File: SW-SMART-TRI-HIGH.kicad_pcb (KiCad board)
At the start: 2 copper layers, 72 x 69 mm, 53 parts, among them J1 SWLINK, J2 USART1, J3 POWER_OUT, SW0 BTS7002-1EPP, SW1 BTS7002-1EPP, SW2 BTS7002-1EPP, U1 STM32G0B1KBTx, U4 MCP2562-E-SN

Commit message: fattened up some tracks
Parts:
- J3: value POWER_OUT -> POWER OUT
- J4: renamed from POWER_IN1; value PWRIN -> POWER IN
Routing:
- net /SW2OUT: vias 0 -> 20
- net /SW1OUT: vias 0 -> 20
- net /SW0OUT: vias 0 -> 21

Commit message: switch to smps for 5v, adjust CAN and SWD pin connections
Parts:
- removed C5V0: 10u, Capacitor_SMD:C_0805_2012Metric_Pad1.18x1.45mm_HandSolder
- removed CVIN1: 10u, Capacitor_SMD:C_1206_3216Metric_Pad1.33x1.80mm_HandSolder
- removed VR5V0: NCV1117ST50, PCM_SparkFun-Semiconductor-Standard:SOT-223-3_TabPin2
- added C15: 100n, Capacitor_SMD:C_0603_1608Metric_Pad1.08x0.95mm_HandSolder, F.Cu at (120.5, 117.9)
- added CIN1: 10u, Capacitor_SMD:C_1210_3225Metric_Pad1.33x2.70mm_HandSolder, F.Cu at (125.7, 128.3)
- added CIN2: 100n, Capacitor_SMD:C_0603_1608Metric_Pad1.08x0.95mm_HandSolder, F.Cu at (120.5, 120.4)
- added COUT3: 10u, Capacitor_SMD:C_0805_2012Metric_Pad1.18x1.45mm_HandSolder, F.Cu at (133.4, 118.1)
- added COUT4: 10u, Capacitor_SMD:C_0805_2012Metric_Pad1.18x1.45mm_HandSolder, F.Cu at (133.4, 121.1)
- added L1: 8.2 uH 55.2 mOhm, SamacSys_Parts:SRP5030HMT2R2M, F.Cu at (126.8, 121.4)
- added RFBB1: 22K1, Resistor_SMD:R_0603_1608Metric_Pad0.98x0.95mm_HandSolder, F.Cu at (120.5, 122.9)
- added RFBT1: 115K, Resistor_SMD:R_0603_1608Metric_Pad0.98x0.95mm_HandSolder, F.Cu at (120.5, 125.4)
- added U3: LMR54410, Package_TO_SOT_SMD:SOT-23-6, F.Cu at (131.3, 128.6)
- CAN1: value H GND L -> G H L; footprint TerminalBlock_Phoenix:TerminalBlock_Phoenix_MKDS-1,5-3-5.08_1x03_P5.08mm_Horizontal -> TerminalBlock_Phoenix:TerminalBlock_Phoenix_MPT-0,5-3-2.54_1x03_P2.54mm_Horizontal
- moved C3V0 8.63 mm to (142.2, 123.8)
- moved CDIV1 5.90 mm to (123.4, 110.4)
- moved RVDIV1 5.90 mm to (123.4, 113.4)
- moved RVDIV2 5.90 mm to (123.4, 111.9)
- moved VR3V3 5.37 mm to (137.6, 127.8), turned to 0 degrees
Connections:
- CAN1 pad 1: /CAN_H -> GND
- CAN1 pad 2: GND -> /CAN_H
- J1 pad 1: +3.3V -> /NRST
- J1 pad 2: /NRST -> +3.3V
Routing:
- net +5V: track 62.3 -> 27.1 mm
- net /VS: track 20.5 -> 4.70 mm
- net GND: track 99.5 -> 86.7 mm, vias 24 -> 22
- net +3.3V: track 70.0 -> 57.4 mm
- net +12V: track 3.03 -> 0.00 mm
- net /NRST: track 16.7 -> 15.9 mm, vias 2 -> 1

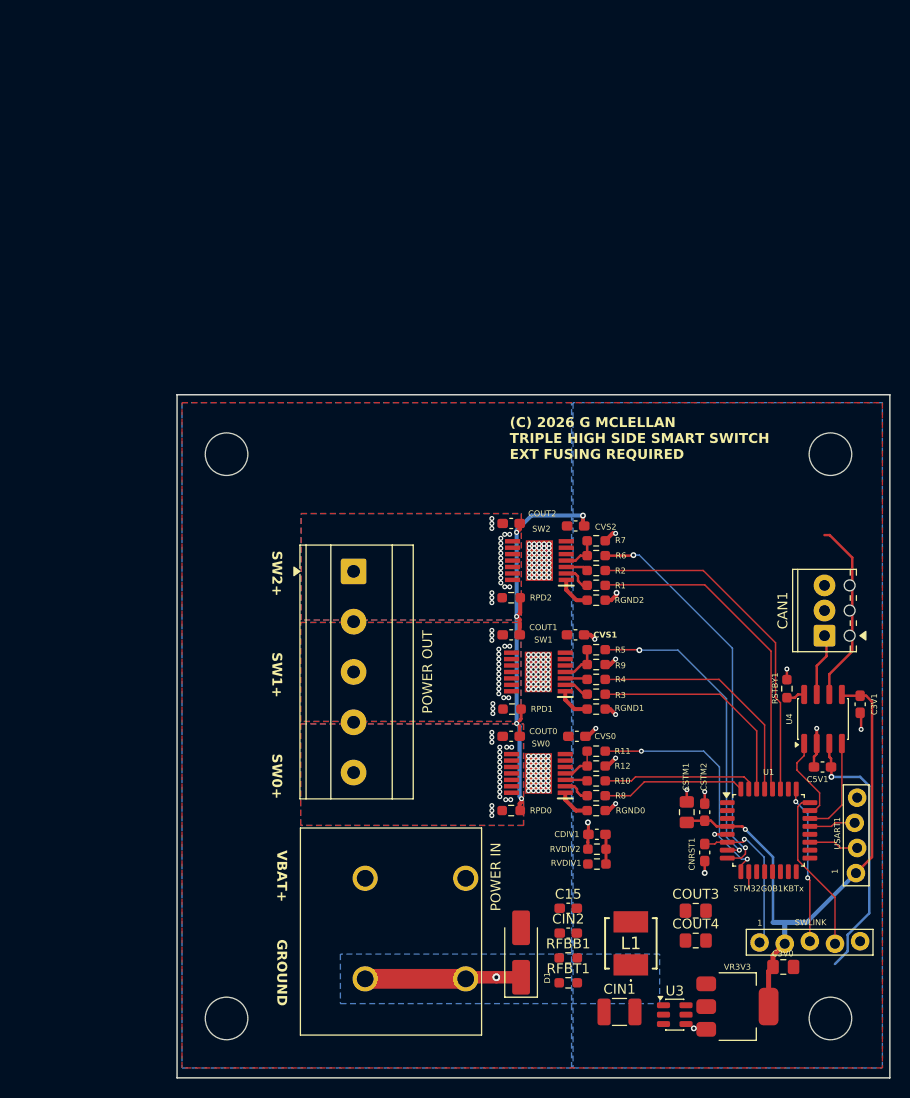
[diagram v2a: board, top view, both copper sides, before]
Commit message: improve ground connections, cleanup silkscreen
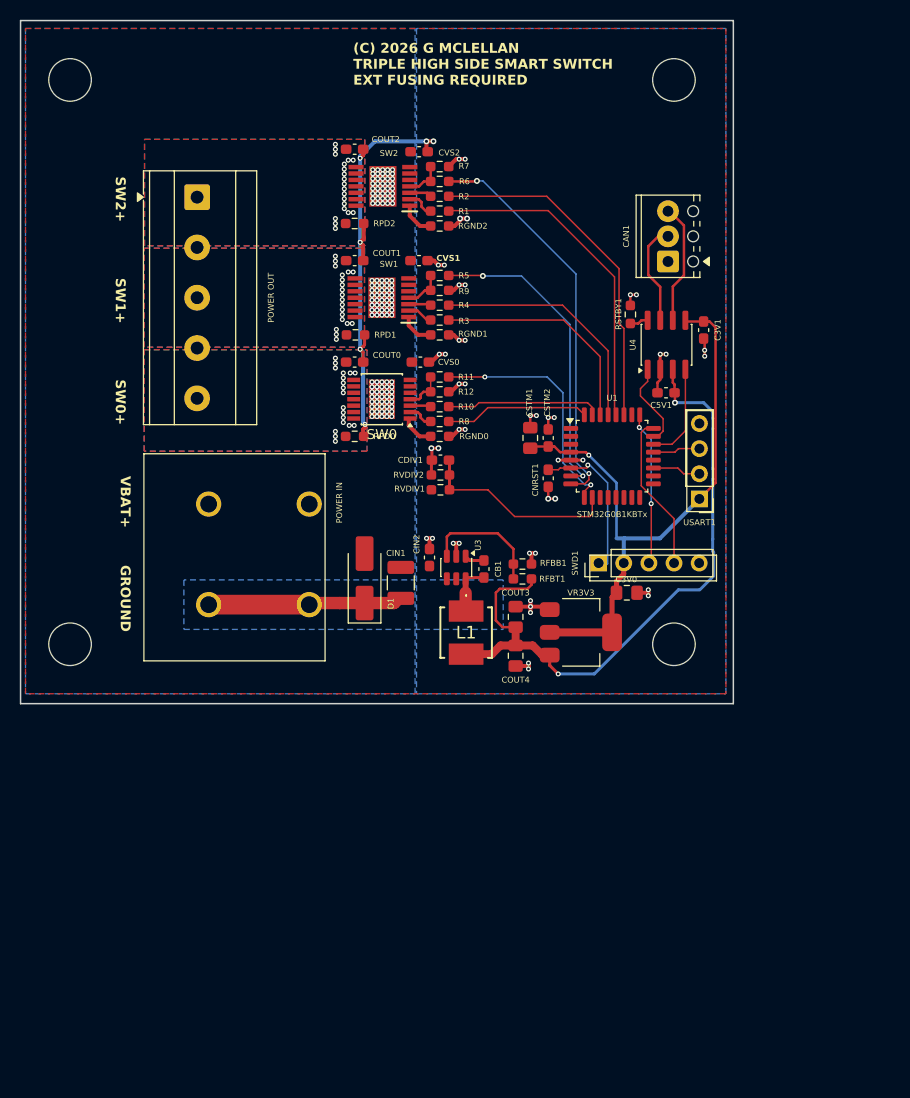
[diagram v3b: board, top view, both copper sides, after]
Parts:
- SW0: footprint SamacSys_Parts:SOP65P600X115-15N -> Package_SO:Infineon_PG-TSDSO-14-22
- SWD1: renamed from J1; value SWLINK -> RST 3V3 CLK DIO GND; footprint PCM_SparkFun-Connector:1x05_P2.54mm_Locking -> Connector_PinHeader_2.54mm:PinHeader_1x05_P2.54mm_Vertical
- USART1: renamed from J2; value USART1 -> 3V3 TX RX GND; footprint PCM_SparkFun-Connector:1x04_P2.54mm_Locking -> Connector_PinHeader_2.54mm:PinHeader_1x04_P2.54mm_Vertical
- moved U3 50.3 mm to (109.2, 83.5), turned to -90 degrees
- moved CIN1 48.6 mm to (103.6, 85.0), turned to -90 degrees
- moved SWD1 41.6 mm to (123.6, 83.0), turned to 90 degrees
- moved RFBT1 41.1 mm to (115.9, 84.6), turned to 180 degrees
- moved CDIV1 41.0 mm to (107.6, 72.6)
- moved RVDIV1 41.0 mm to (107.6, 75.6)
- moved RVDIV2 41.0 mm to (107.6, 74.1)
- moved C3V1 41.0 mm to (134.2, 59.5)
- moved J3 41.0 mm to (83.0, 46.0)
- moved C3V0 41.0 mm to (126.4, 86.0)
- moved CAN1 41.0 mm to (130.6, 52.5)
- moved CNRST1 41.0 mm to (118.5, 74.4)
- moved COUT0 41.0 mm to (98.9, 62.7)
- moved COUT1 41.0 mm to (98.9, 52.5)
- moved COUT2 41.0 mm to (98.9, 41.2)
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- renumbered C15 to CB1
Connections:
- net Net-(U3-FB) renamed /FB
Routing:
- net +5V: track 27.1 -> 67.0 mm
- net GND: track 86.7 -> 113.0 mm, vias 22 -> 51
- net /VS: track 4.70 -> 20.3 mm
- net /FB: track 0.00 -> 12.5 mm
- net /CAN_L: track 18.6 -> 12.2 mm
- net +3.3V: track 57.4 -> 63.2 mm
- net /SW: track 0.00 -> 4.94 mm
- net /CAN_H: track 6.43 -> 10.4 mm
- net /CB: track 0.00 -> 2.03 mm
- net /SW0IS_PD: track 4.02 -> 4.81 mm
- net /SWDIO: track 16.8 -> 16.2 mm
- net /SW0IS: track 24.6 -> 23.9 mm
- net /SW0OUT: vias 21 -> 19
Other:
- board text removed: "1"

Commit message: fixed some footprints, made the +12v pour a bit bigger on the bottom side
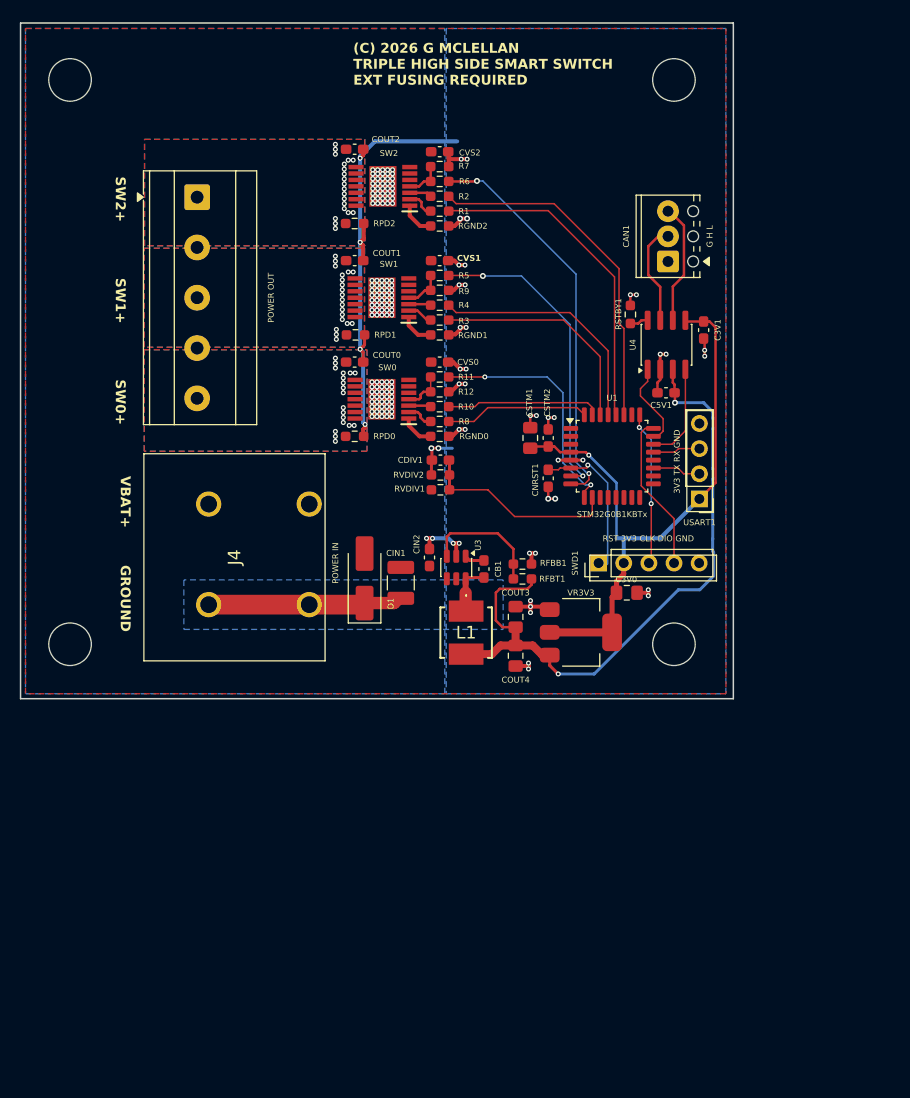
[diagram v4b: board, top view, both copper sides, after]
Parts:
- SW0: footprint Package_SO:Infineon_PG-TSDSO-14-22 -> SamacSys_Parts:SOP65P600X115-15N
- moved CVS1 2.08 mm to (107.5, 52.5)
- moved CVS2 2.08 mm to (107.5, 41.5)
- moved CVS0 1.95 mm to (107.5, 62.7)
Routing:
- net GND: track 113.0 -> 121.0 mm, vias 51 -> 49
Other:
- board size 72 x 69 mm -> 72 x 68.2 mm

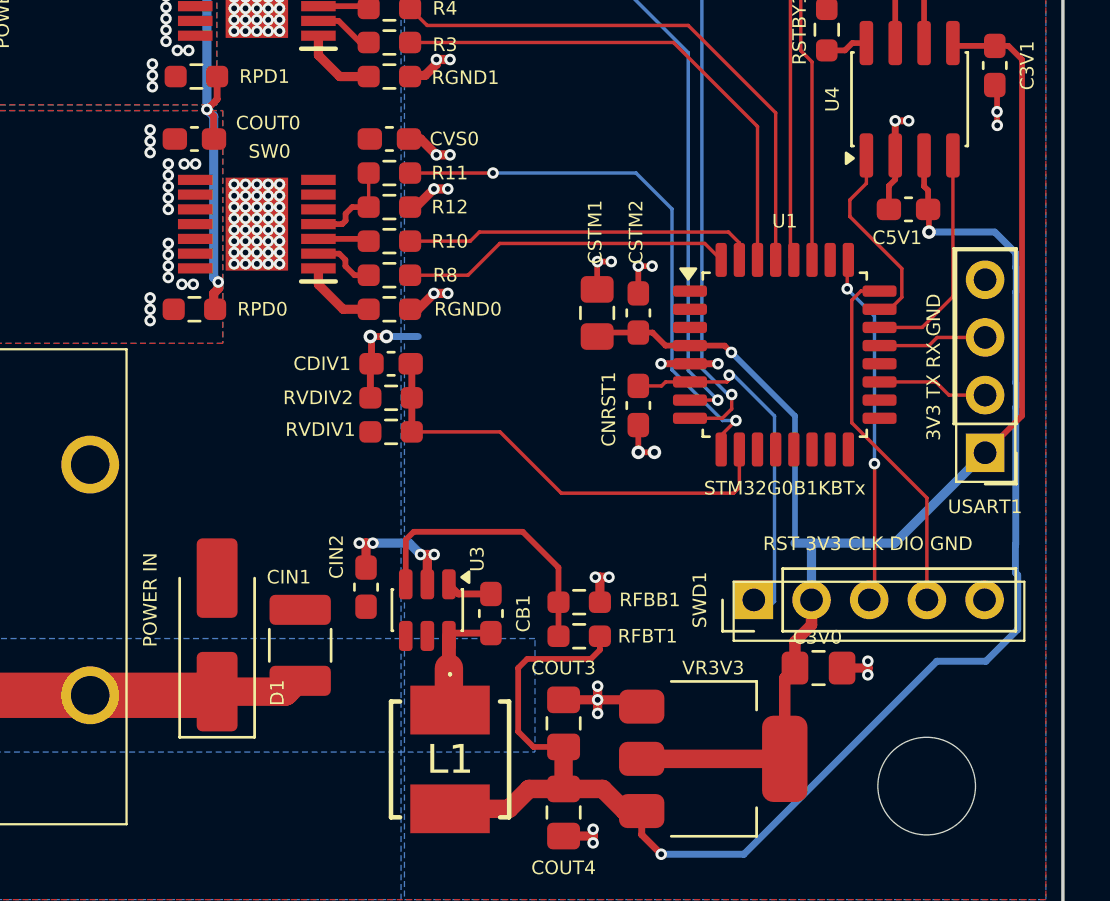
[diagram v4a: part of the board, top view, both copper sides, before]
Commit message: add 8mhz XO, fix some footprint issues
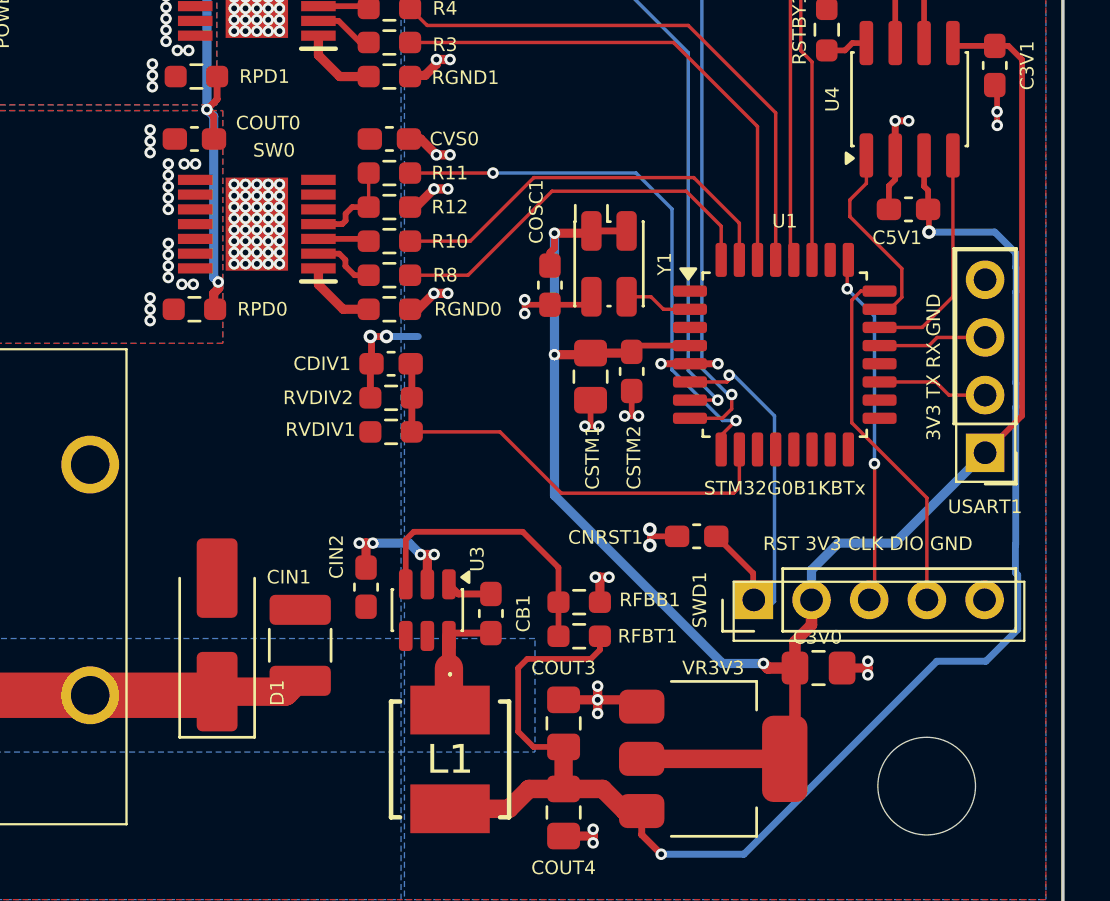
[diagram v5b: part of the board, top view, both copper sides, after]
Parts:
- added COSC1: 100n, Capacitor_SMD:C_0603_1608Metric_Pad1.08x0.95mm_HandSolder, F.Cu at (114.6, 69.1)
- added Y1: 8MHz, 3525_4pin_OSC:Oscillator_SMD_XO-4Pin_3.2x2.5mm_HandSoldering, F.Cu at (117.2, 68.2)
- moved CNRST1 6.31 mm to (121.1, 80.2), turned to 180 degrees
- moved CSTM1 2.82 mm to (116.4, 73.2), turned to -90 degrees
- moved CSTM2 2.59 mm to (118.2, 72.9), turned to -90 degrees
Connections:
- U1 pad 2: unconnected-(U1-PC14-Pad2) -> /OSC
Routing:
- net +3.3V: track 63.2 -> 82.2 mm, vias 1 -> 3
- net GND: track 121.0 -> 124.5 mm, vias 49 -> 51
- net /OSC: track 0.00 -> 3.02 mm
- net /SW0IN: track 14.6 -> 17.4 mm
- net /SW0DEN: track 15.6 -> 18.1 mm
- net /NRST: track 15.9 -> 17.0 mm
